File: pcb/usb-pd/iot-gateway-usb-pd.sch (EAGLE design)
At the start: 39 parts, among them CON1 2P-PH-TOP, CON2 6P-SH-TOP, CON3 3P-SH-TOP, CON4 5P-SH-TOP, J1 DCJACK, Q1 AO3401, Q2 AO3401, U1 FUSB302MPX, U2 74LVC1G04, U3 74LVC1G08, U4 MIC2019, U5 LTC4412

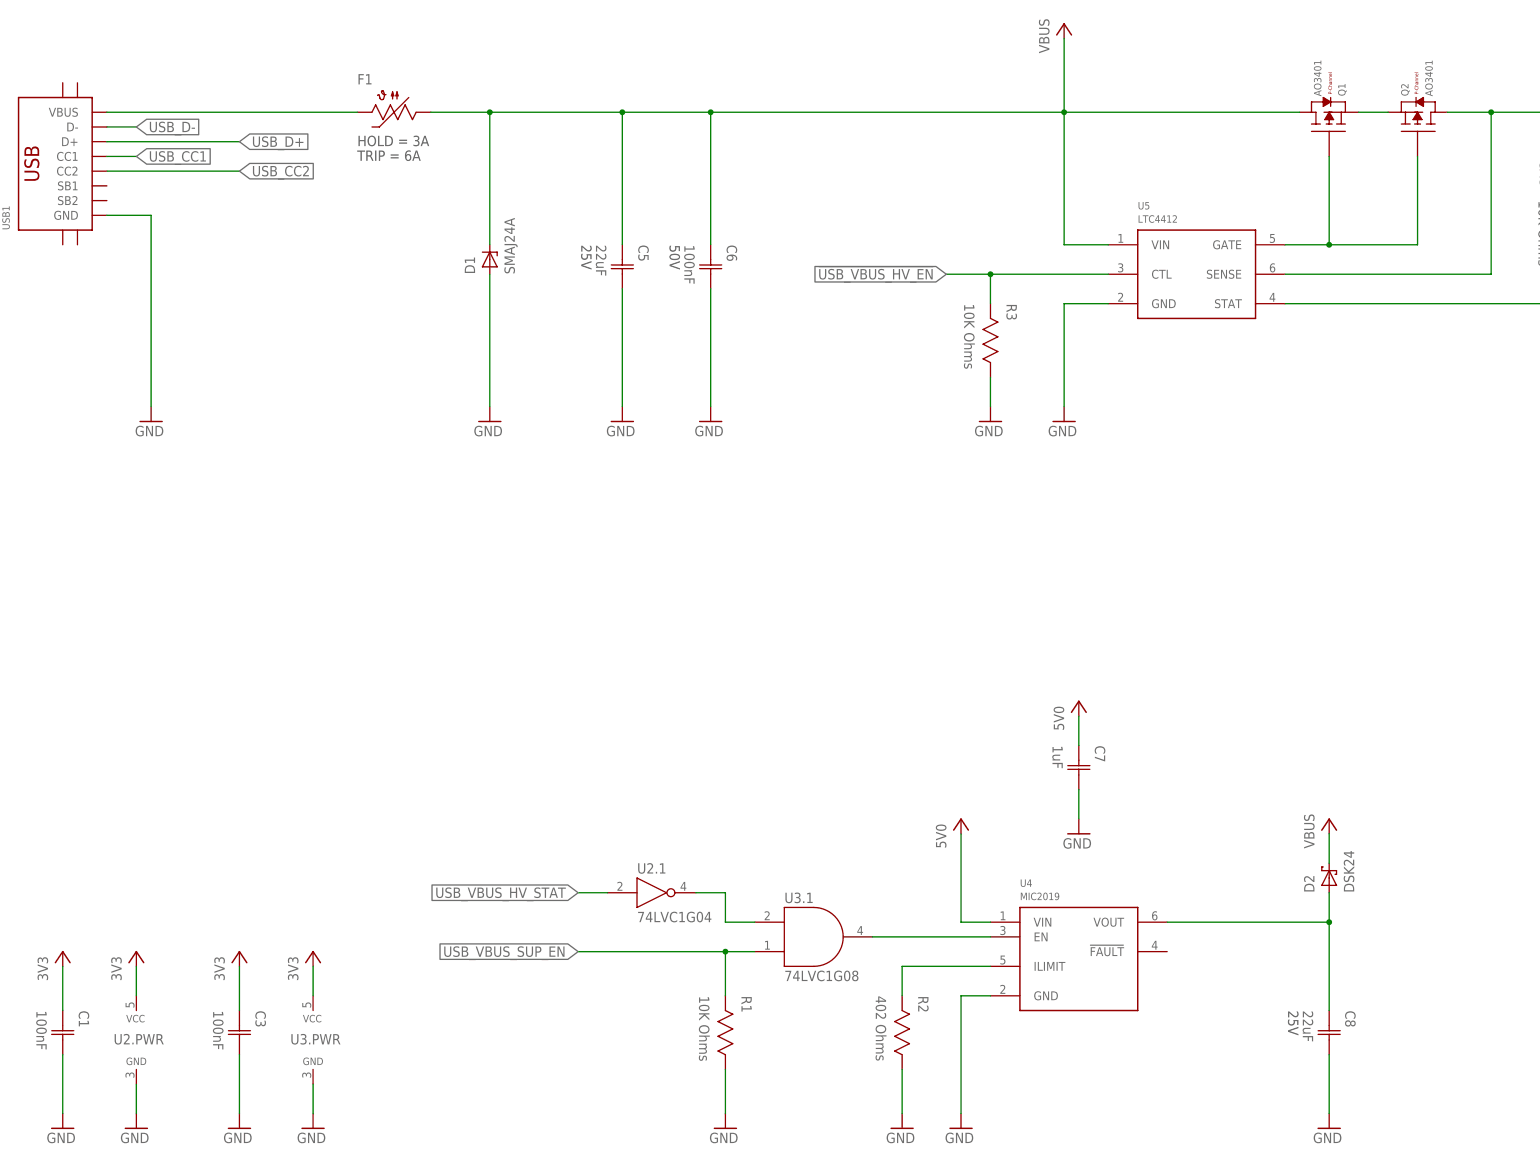
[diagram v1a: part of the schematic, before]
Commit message: Update libraries Finish routing Generate schematic PDF files
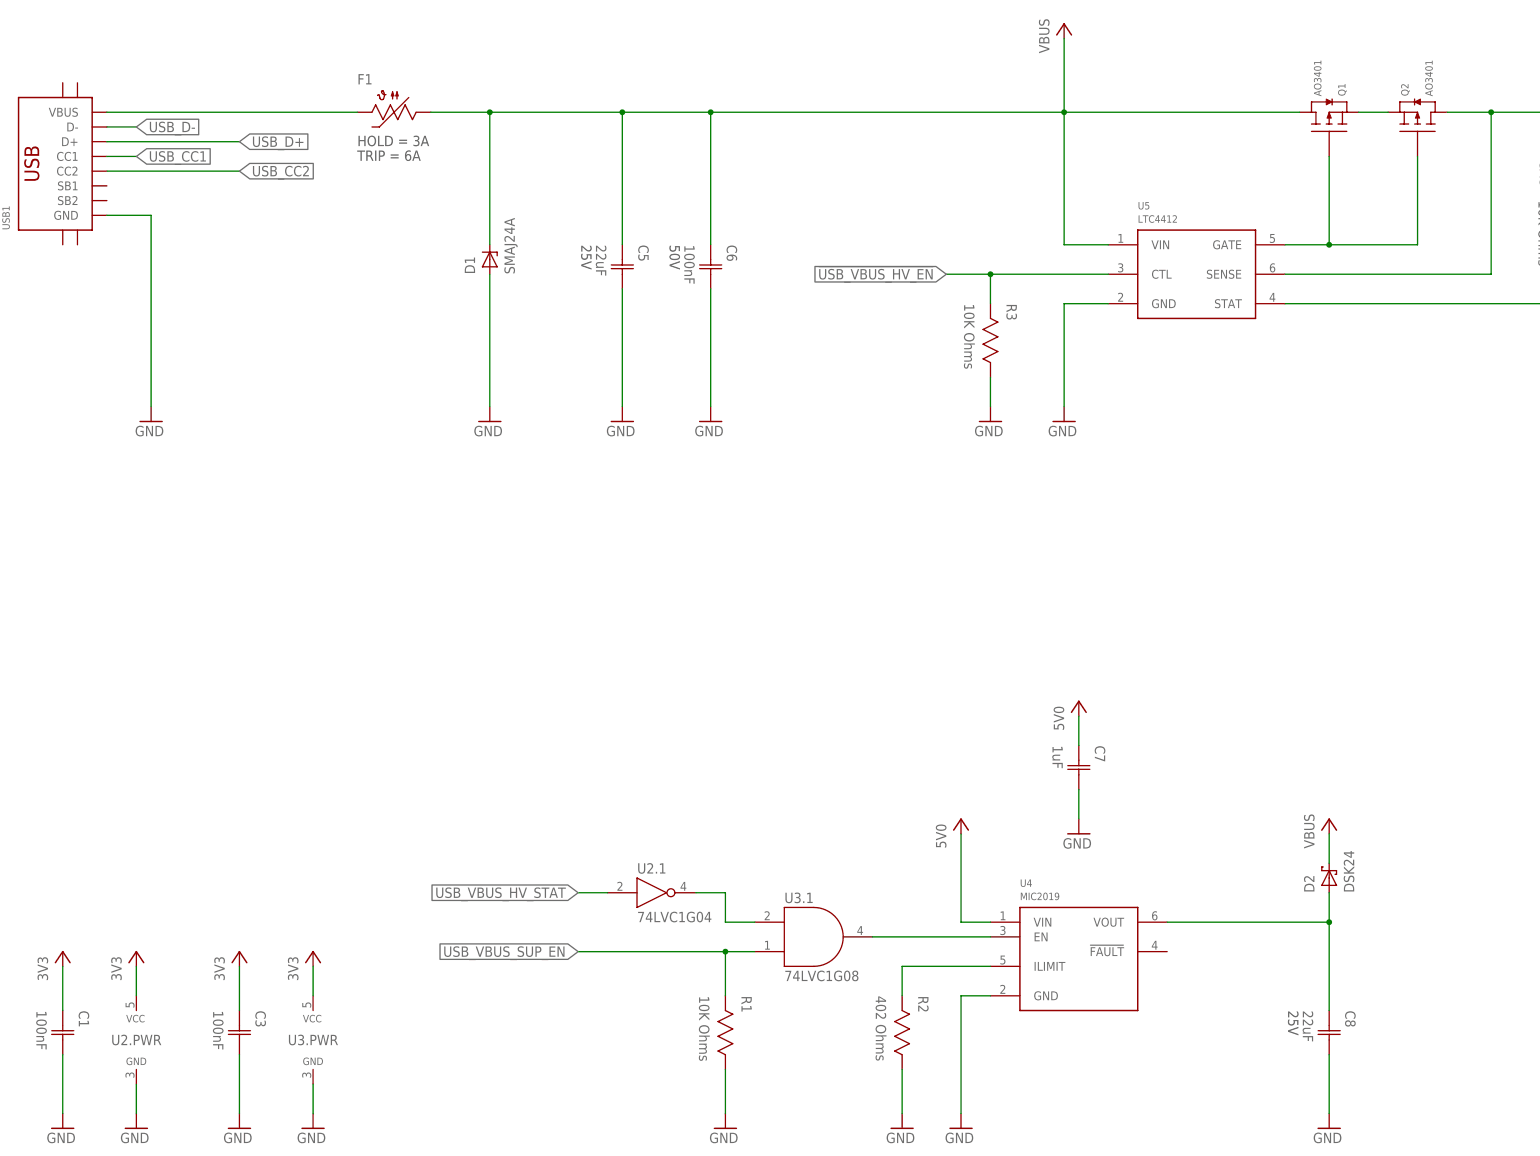
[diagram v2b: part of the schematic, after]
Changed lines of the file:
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@@
 </instance>
 <instance part="U2" gate=".PWR" x="58.42" y="187.96" smashed="yes">
-<attribute name="NAME" x="54.483" y="187.198" size="1.778" layer="95"/>
+<attribute name="NAME" x="58.42" y="187.96" size="1.778" layer="95" align="center"/>
 </instance>
 <instance part="U2" gate=".1" x="149.86" y="213.36" smashed="yes">
@@
 </instance>
 <instance part="U3" gate=".PWR" x="88.9" y="187.96" smashed="yes">
-<attribute name="NAME" x="84.963" y="187.198" size="1.778" layer="95"/>
+<attribute name="NAME" x="88.9" y="187.96" size="1.778" layer="95" align="center"/>
 </instance>
 <instance part="C4" gate="G$1" x="81.28" y="40.64" smashed="yes" rot="R270">
